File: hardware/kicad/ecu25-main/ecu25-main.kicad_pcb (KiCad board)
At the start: 2 copper layers, 200 x 150 mm, 306 parts, among them J1 Screw_Terminal_BATT, J10 Screw_Terminal_RS485, J11 TC2030 SWD, J12 Ribbon 20-way, J13 Screw_Terminal_DPLUS, J14 DEBUG_UART, J15 Screw_Terminal_CONTACTOR, J2 Screw_Terminal_DIN, J3 Screw_Terminal_SENDERS, J4 Screw_Terminal_MPU, J5 Screw_Terminal_GEN, J6 Screw_Terminal_MAINS, J7 Screw_Terminal_CT, J8 Screw_Terminal_RELAY_OUT, J9 Screw_Terminal_CAN, K1 G5LE-1 12V, K2 G5LE-1 12V, K3 G5LE-1 12V, K4 G5LE-1 12V, K5 G5LE-1 12V, K6 G5LE-1 12V, Q1 SQD50P06-15L, Q3 BC857, Q4 BC857, Q5 BC857, Q60 2N7002K 60V, Q61 2N7002K 60V, Q62 2N7002K 60V, Q63 2N7002K 60V, Q64 2N7002K 60V, Q65 2N7002K 60V, U1 LM5164DDA-Q1, U10 MCP6002, U11 M95M02-DR, U12 STM32F407VGT6, U2 TLV75533 (500mA), U3 LM358, U4 LM358, U5 LM2903, U6 TJA1051T/3, U7 THVD1450, U8 MCP6002, U9 MCP6002, Y1 8MHz, Y2 32.768kHz

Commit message: Fix SME verification findings; add COT ripple injection and the I/O map
An independent verification pass re-derived the 12 V conversion fixes against
the TI, Omron, Nexperia and ST datasheets instead of trusting the commit
message. The hold-up energy math, the RON/UVLO arithmetic, the modbus_rx
bounds, the AUX refactor and the dry-contact output stage all held. Eleven
majors did not.

Hardware:
- The buck had no ripple-injection network. The LM5164 is constant-on-time:
  it restarts the on-time when FB falls to the 1.2 V reference, so it needs
  >=20 mV of FB ripple IN PHASE with the inductor current. Two 22 uF ceramics
  give 2.7 mV, and that component is capacitive, i.e. out of phase — the
  required series ESR would be 0.287 ohm against the ~2 mohm they actually
  have. The part would have burst-switched: several on-times in close
  succession then a long off-time. Added the datasheet's Type-3 network
  (R7 100k, C10 4.7nF, C11 1nF C0G), which builds the ramp from SW and
  couples it into FB, leaving output ripple untouched. 21 mV at 12.6 V in,
  13 mV at 8 V, against a 12 mV floor
- DIN ground-side pull-up 2.2k -> 1k. 2.2k sat at 2.25 V at 12.6 V but fell
  to 1.59 V during an 8.5 V crank sag — back inside the STM32's indeterminate
  band. The value has to be set by the worst case: V_bat x 1.8/(R+7.4) needs
  R <= 670 ohm to clear V_IH 1.785 V at 8.0 V
- The hold-up node was still the autogenerated Net-(D3-K), so the netclass
  rule and the DRU keyed off a reference designator. Now labelled +12V_HLD
- C9 25 V -> 35 V never reached the orderable BOM: gen_bom.py still said
  "2200 uF 25 V radial" for a node the design puts at 25.6 V
- OUT_COM moved to the Battery class and given a stated ceiling: 4 A total,
  2 A per output, installer fuse 4 A. Four 8 A contacts on a trunk sized for
  4 A needed writing down; it was implied by the netclass and nowhere else
- gen_pcb.py netclass assertion rewritten. It was blind to exactly the
  suffix patterns it was written to pr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
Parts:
- added C10: 4.7nF C0G, C_0603_1608Metric, F.Cu at (86.7, 37.4)
- added C11: 1nF C0G, C_0603_1608Metric, F.Cu at (91.0, 37.4)
- added R7: 100k 1%, R_0603_1608Metric, F.Cu at (38.1, 51.2)
- R231, R232, R233, R234, R235, R236, R237, R238: value 2.2k 0.5W -> 1k 0.5W
- moved C7 54.5 mm to (92.6, 43.1)
- moved R3 54.5 mm to (92.6, 45.8)
- moved R6 54.5 mm to (92.6, 48.5)
- moved R1 50.4 mm to (38.1, 45.8)
- moved R4 50.4 mm to (38.1, 48.5)
- moved C2 49.0 mm to (38.1, 43.1)
- moved C4 6.28 mm to (88.4, 43.1)
- moved R2 5.01 mm to (88.4, 45.8)
- moved R5 5.01 mm to (88.4, 48.5)
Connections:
- net Net-(D3-K) renamed /Power/+12V_HLD
- net Net-(U1-SW) renamed /Power/BUCK_SW

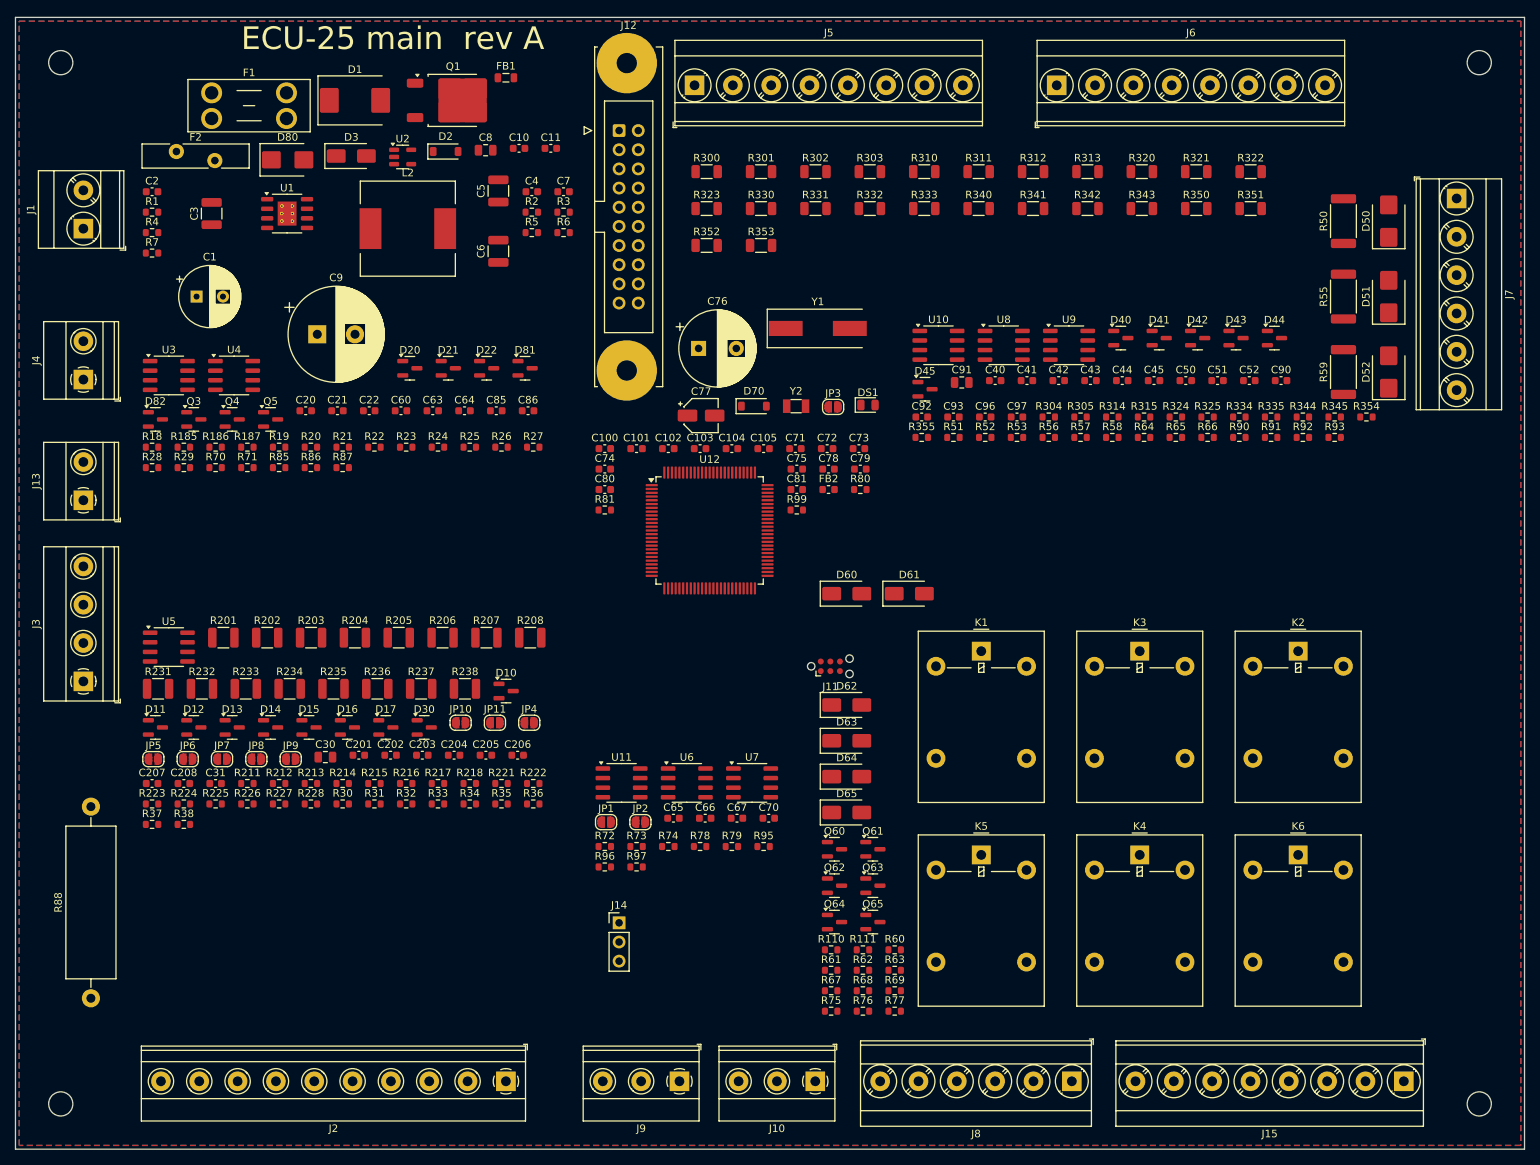
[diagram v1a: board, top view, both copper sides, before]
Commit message: Fix PCB routing: pour keepouts blocked the router; add HV clearance gate
The board would not autoroute past ~20% and the cause was not density.
KiCad's Specctra exporter writes every rule area as a bare (keepout ...),
losing the distinction between "no copper pour here" and "no traces here".
This board's rule areas are pour-only — they exist to hold the ground pour
out of the HV zone — so the router was locked out of 74 cm2 of a 300 cm2
board containing 98 pads: the whole R300-R353 divider chain, the K2/K3/K4/K6
relays and the J5/J6/J8/J15 mains terminals. Dropping the pour-only rule
areas at export time takes the 2-layer board from 376 unrouted to 154.

Creepage is unaffected: HV spacing is carried by the netclass clearances
(HV_AC 3 mm, HV_CHAIN 1 mm), which the DSN keeps.

The optimizer is now switched off. Freerouting warns on every run that
"Multi-threaded route optimization is broken and it is known to generate
clearance violations", and -mt 1 alone did not suppress it. It was not
theoretical: an optimized board came back with 338 violations of the 415 V
rules, the worst 2.869 mm where 3.0 mm is required. With the optimizer off
there are none, at a cost of 85 unrouted connections and no measurable
change in score. The remainder is finished by hand in pcbnew.

check_hv_clearance.py is a headless verifier for that rule, since kicad-cli
7 has no DRC subcommand. It reads the netclass clearances from the board and
the custom rules from the .kicad_dru rather than carrying its own copy, and
refuses to run on rule syntax it cannot parse instead of skipping it.
route_pcb.py now runs it as a gate and fails the pipeline on a violation,
where it previously printed a report nobody read and exited 0 regardless.

Two pcbnew traps documented at their call sites: removing zones from a board
poisons the module for the rest of the process, so every later LoadBoard()
returns a bare SwigPyObject — the import and the check therefore run as
subprocesses. And freerouting flushes its 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
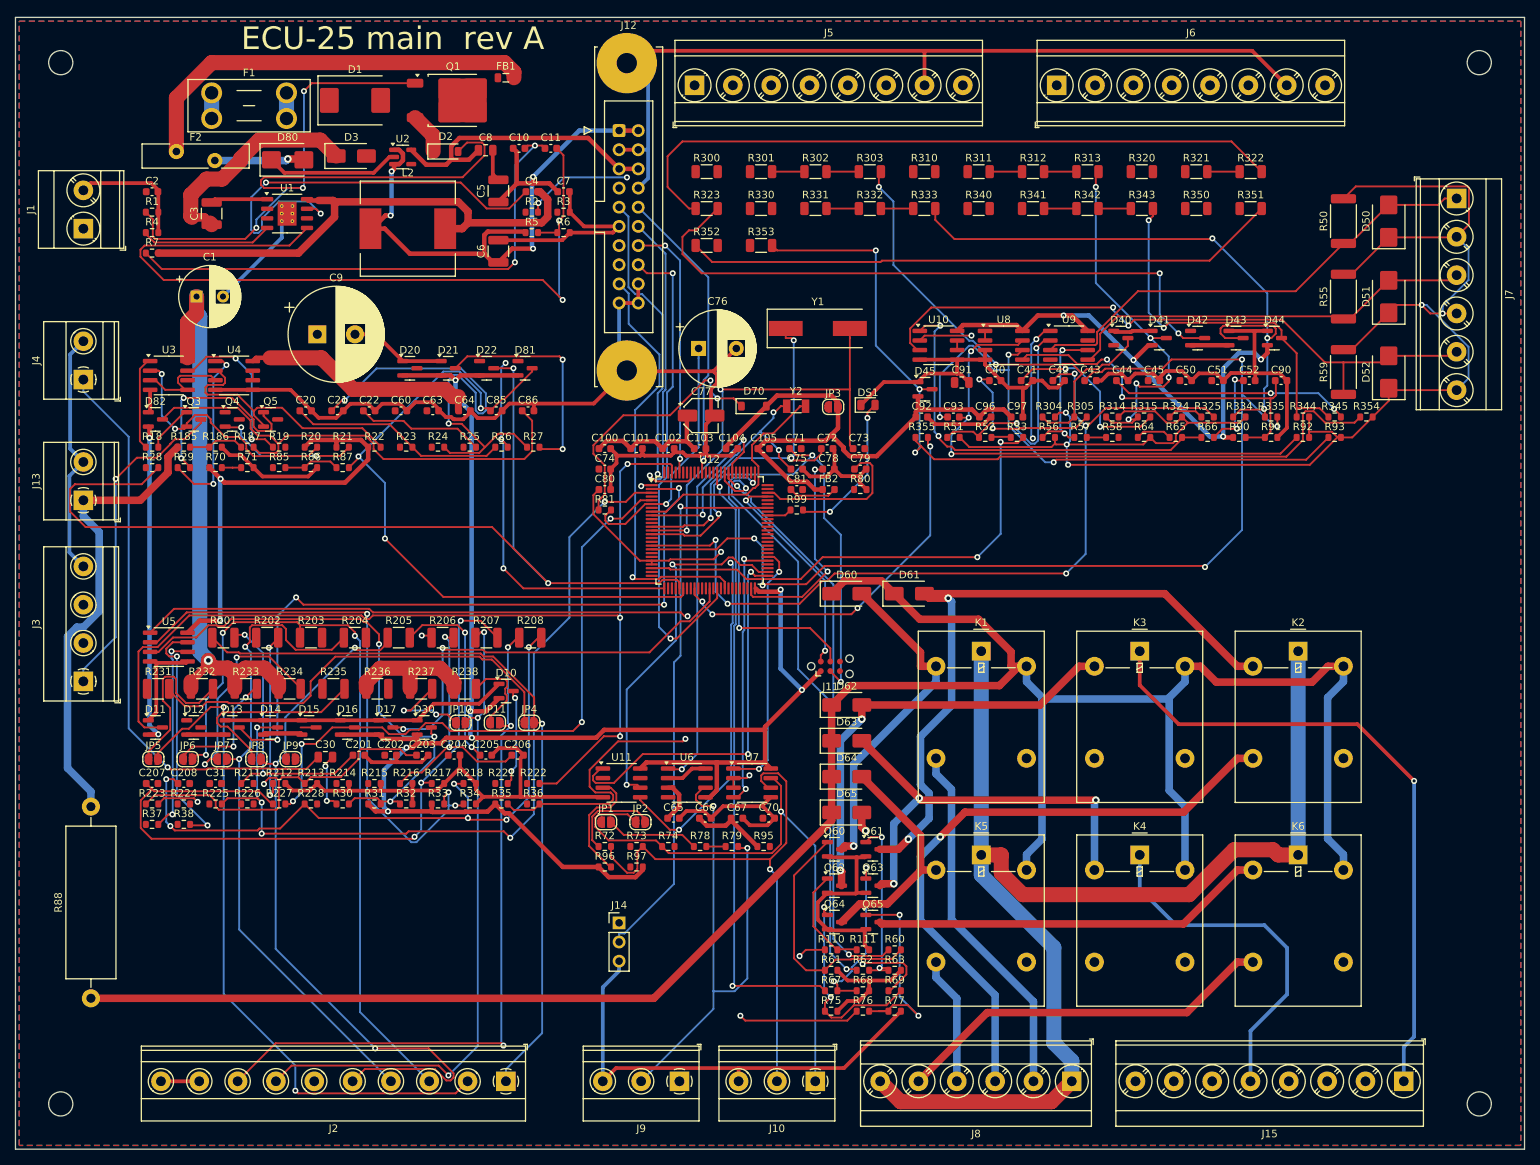
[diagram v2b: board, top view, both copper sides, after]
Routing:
- net GND: track 0.00 -> 791.4 mm
- net +3V3: track 0.00 -> 509.7 mm, vias 0 -> 13
- net +12V_SW: track 0.00 -> 320.2 mm, vias 0 -> 1
- net VREF_MID: track 0.00 -> 212.8 mm, vias 0 -> 5
- net +12V: track 0.00 -> 180.7 mm, vias 0 -> 1
- net /Relay drivers/OUT_COM: track 0.00 -> 165.0 mm
- net +5V: track 0.00 -> 152.2 mm, vias 0 -> 6
- net ACV_MAINS_L1: track 0.00 -> 139.9 mm, vias 0 -> 5
- net DIN2: track 0.00 -> 135.8 mm, vias 0 -> 3
- net ADC_TEMP: track 0.00 -> 134.7 mm, vias 0 -> 2
- net ACV_GEN_L3: track 0.00 -> 114.3 mm, vias 0 -> 5
- net DIN5: track 0.00 -> 112.8 mm, vias 0 -> 5
- net Net-(D45-K-Pad3): track 0.00 -> 112.2 mm, vias 0 -> 3
- net MPU_RPM: track 0.00 -> 108.6 mm, vias 0 -> 2
- net /Power/BUCK_FB: track 0.00 -> 107.7 mm, vias 0 -> 2
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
